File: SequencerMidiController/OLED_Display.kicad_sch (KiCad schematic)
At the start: 5 parts, among them J8 Conn_01x07

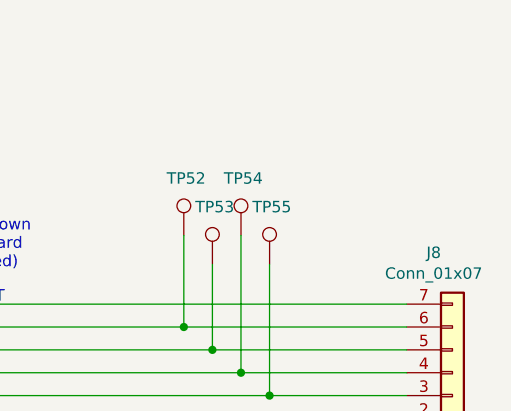
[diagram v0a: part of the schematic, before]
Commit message: Add ground points
https://github.com/cracked-machine/BassStationSequencerMidiController/issues/9

Also, made space on layout for uSDCard IDC connector and DAC analog output section
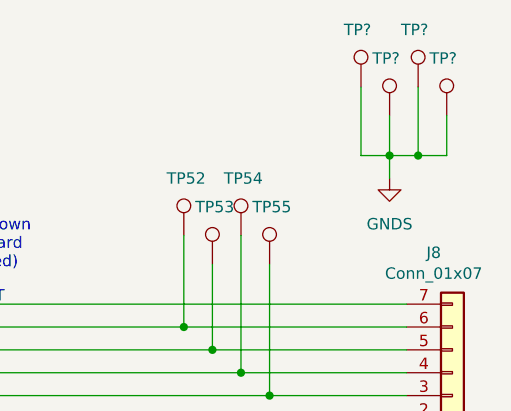
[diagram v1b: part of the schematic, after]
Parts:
- added TP? (x4): TestPoint, TestPoint:TestPoint_Pad_D1.0mm, symbol Connector:TestPoint
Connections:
- net GNDS: now also TP?.1, TP?.1, TP?.1, TP?.1
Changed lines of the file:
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@@
   (junction (at 130.81 86.36) (diameter 0) (color 0 0 0 0)
   )
+  (junction (at 153.67 64.77) (diameter 0) (color 0 0 0 0)
+  )
   (junction (at 133.985 88.9) (diameter 0) (color 0 0 0 0)
+  )
+  (junction (at 150.495 64.77) (diameter 0) (color 0 0 0 0)
   )
   (no_connect (at 87.63 81.28))
@@
     (stroke (width 0) (type default) (color 0 0 0 0))
   )
+  (wire (pts (xy 150.495 64.77) (xy 153.67 64.77))
+    (stroke (width 0) (type default) (color 0 0 0 0))
+  )
   (wire (pts (xy 152.4 83.82) (xy 127.635 83.82))
     (stroke (width 0) (type default) (color 0 0 0 0))
   )
+  (wire (pts (xy 156.845 64.77) (xy 156.845 60.325))
+    (stroke (width 0) (type default) (color 0 0 0 0))
+  )
   (wire (pts (xy 152.4 93.98) (xy 87.63 93.98))
     (stroke (width 0) (type default) (color 0 0 0 0))
   )
+  (wire (pts (xy 147.32 64.77) (xy 150.495 64.77))
+    (stroke (width 0) (type default) (color 0 0 0 0))
+  )
   (wire (pts (xy 133.985 88.9) (xy 87.63 88.9))
     (stroke (width 0) (type default) (color 0 0 0 0))
   )
+  (wire (pts (xy 150.495 60.325) (xy 150.495 64.77))
+    (stroke (width 0) (type default) (color 0 0 0 0))
+  )
+  (wire (pts (xy 153.67 64.77) (xy 156.845 64.77))
+    (stroke (width 0) (type default) (color 0 0 0 0))
+  )
   (wire (pts (xy 152.4 88.9) (xy 133.985 88.9))
     (stroke (width 0) (type default) (color 0 0 0 0))
   )
+  (wire (pts (xy 147.32 57.15) (xy 147.32 64.77))
+    (stroke (width 0) (type default) (color 0 0 0 0))
+  )
   (wire (pts (xy 87.63 81.28) (xy 152.4 81.28))
     (stroke (width 0) (type default) (color 0 0 0 0))
@@
     (stroke (width 0) (type default) (color 0 0 0 0))
   )
+  (wire (pts (xy 153.67 57.15) (xy 153.67 64.77))
+    (stroke (width 0) (type default) (color 0 0 0 0))
+  )
   (wire (pts (xy 152.4 96.52) (xy 111.76 96.52))
     (stroke (width 0) (type default) (color 0 0 0 0))
@@
   )
   (wire (pts (xy 152.4 91.44) (xy 137.16 91.44))
+    (stroke (width 0) (type default) (color 0 0 0 0))
+  )
+  (wire (pts (xy 150.495 64.77) (xy 150.495 67.31))
     (stroke (width 0) (type default) (color 0 0 0 0))
   )
@@
       (effects (font (size 1.27 1.27)) hide)
     )
+    (pin "1")
+  )
+  (symbol (lib_id "Connector:TestPoint") (at 150.495 60.325 0) (unit 1)
+    (in_bom yes) (on_board yes)
+    (property "Reference" "TP?" (id 0) (at 148.59 53.975 0)
+      (effects (font (size 1.27 1.27)) (justify left))
+    )
+    (property "Value" "TestPoint" (id 1) (at 151.9682 59.6392 0)
+      (effects (font (size 1.27 1.27)) (justify left) hide)
+    )
+    (property "Footprint" "TestPoint:TestPoint_Pad_D1.0mm" (id 2) (at 155.575 60.325 0)
+      (effects (font (size 1.27 1.27)) hide)
+    )
+    (property "Datasheet" "~" (id 3) (at 155.575 60.325 0)
+      (effects (font (size 1.27 1.27)) hide)
+    )
+    (property "LcscNo" "~" (id 4) (at 150.495 60.325 0)
+      (effects (font (size 1.27 1.27)) hide)
+    )
+    (property "Type" "~" (id 5) (at 150.495 60.325 0)
+      (effects (font (size 1.27 1.27)) hide)
+    )
+    (pin "1")
+  )
+  (symbol (lib_id "Connector:TestPoint") (at 156.845 60.325 0) (unit 1)
+    (in_bom yes) (on_board yes)
+    (property "Reference" "TP?" (id 0) (at 154.94 53.975 0)
+      (effects (font (size 1.27 1.27)) (justify left))
+    )
+    (property "Value" "TestPoint" (id 1) (at 158.3182 59.6392 0)
+      (effects (font (size 1.27 1.27)) (justify left) hide)
+    )
+    (property "Footprint" "TestPoint:TestPoint_Pad_D1.0mm" (id 2) (at 161.925 60.325 0)
+      (effects (font (size 1.27 1.27)) hide)
+    )
+    (property "Datasheet" "~" (id 3) (at 161.925 60.325 0)
+      (effects (font (size 1.27 1.27)) hide)
+    )
+    (property "LcscNo" "~" (id 4) (at 156.845 60.325 0)
+      (effects (font (size 1.27 1.27)) hide)
+    )
+    (property "Type" "~" (id 5) (at 156.845 60.325 0)
+      (effects (font (size 1.27 1.27)) hide)
+    )
+    (pin "1")
+  )
+  (symbol (lib_id "Connector:TestPoint") (at 153.67 57.15 0) (unit 1)
+    (in_bom yes) (on_board yes)
+    (property "Reference" "TP?" (id 0) (at 151.765 50.8 0)
+      (effects (font (size 1.27 1.27)) (justify left))
+    )
+    (property "Value" "TestPoint" (id 1) (at 155.1432 56.4642 0)
+      (effects (font (size 1.27 1.27)) (justify left) hide)
+    )
+    (property "Footprint" "TestPoint:TestPoint_Pad_D1.0mm" (id 2) (at 158.75 57.15 0)
+      (effects (font (size 1.27 1.27)) hide)
+    )
+    (property "Datasheet" "~" (id 3) (at 158.75 57.15 0)
+      (effects (font (size 1.27 1.27)) hide)
+    )
+    (property "LcscNo" "~" (id 4) (at 153.67 57.15 0)
+      (effects (font (size 1.27 1.27)) hide)
+    )
+    (property "Type" "~" (id 5) (at 153.67 57.15 0)
+      (effects (font (size 1.27 1.27)) hide)
+    )
+    (pin "1")
+  )
+  (symbol (lib_id "Connector:TestPoint") (at 147.32 57.15 0) (unit 1)
+    (in_bom yes) (on_board yes)
+    (property "Reference" "TP?" (id 0) (at 145.415 50.8 0)
+      (effects (font (size 1.27 1.27)) (justify left))
+    )
+    (property "Value" "TestPoint" (id 1) (at 148.7932 56.4642 0)
+      (effects (font (size 1.27 1.27)) (justify left) hide)
+    )
+    (property "Footprint" "TestPoint:TestPoint_Pad_D1.0mm" (id 2) (at 152.4 57.15 0)
+      (effects (font (size 1.27 1.27)) hide)
+    )
+    (property "Datasheet" "~" (id 3) (at 152.4 57.15 0)
+      (effects (font (size 1.27 1.27)) hide)
+    )
+    (property "LcscNo" "~" (id 4) (at 147.32 57.15 0)
+      (effects (font (size 1.27 1.27)) hide)
+    )
+    (property "Type" "~" (id 5) (at 147.32 57.15 0)
+      (effects (font (size 1.27 1.27)) hide)
+    )
+    (pin "1")
+  )
+  (symbol (lib_id "power:GNDS") (at 150.495 67.31 0) (unit 1)
+    (in_bom yes) (on_board yes) (fields_autoplaced)
+    (property "Reference" "#PWR?" (id 0) (at 150.495 73.66 0)
+      (effects (font (size 1.27 1.27)) hide)
+    )
+    (property "Value" "GNDS" (id 1) (at 150.495 72.39 0))
+    (property "Footprint" "" (id 2) (at 150.495 67.31 0)
+      (effects (font (size 1.27 1.27)) hide)
+    )
+    (property "Datasheet" "" (id 3) (at 150.495 67.31 0)
+      (effects (font (size 1.27 1.27)) hide)
+    )

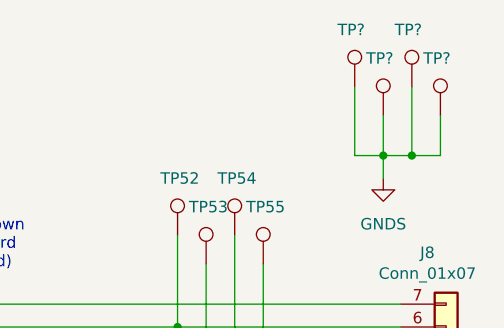
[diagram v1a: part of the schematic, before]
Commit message: updated layout DRC
Fixed clearance errors with polygons and pads in switch footprints
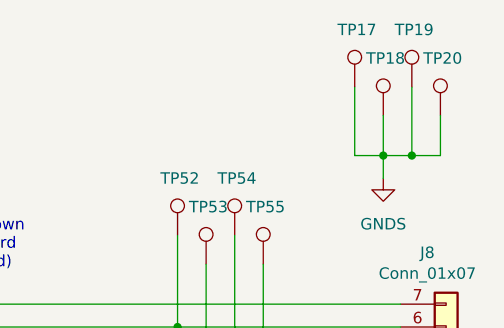
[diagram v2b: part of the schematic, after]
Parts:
- gave numbers to parts that had none: 4
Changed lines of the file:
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@@
   (symbol (lib_id "Connector:TestPoint") (at 150.495 60.325 0) (unit 1)
     (in_bom yes) (on_board yes)
-    (property "Reference" "TP?" (id 0) (at 148.59 53.975 0)
+    (property "Reference" "TP18" (id 0) (at 148.59 53.975 0)
       (effects (font (size 1.27 1.27)) (justify left))
     )
@@
   (symbol (lib_id "Connector:TestPoint") (at 156.845 60.325 0) (unit 1)
     (in_bom yes) (on_board yes)
-    (property "Reference" "TP?" (id 0) (at 154.94 53.975 0)
+    (property "Reference" "TP20" (id 0) (at 154.94 53.975 0)
       (effects (font (size 1.27 1.27)) (justify left))
     )
@@
   (symbol (lib_id "Connector:TestPoint") (at 153.67 57.15 0) (unit 1)
     (in_bom yes) (on_board yes)
-    (property "Reference" "TP?" (id 0) (at 151.765 50.8 0)
+    (property "Reference" "TP19" (id 0) (at 151.765 50.8 0)
       (effects (font (size 1.27 1.27)) (justify left))
     )
@@
   (symbol (lib_id "Connector:TestPoint") (at 147.32 57.15 0) (unit 1)
     (in_bom yes) (on_board yes)
-    (property "Reference" "TP?" (id 0) (at 145.415 50.8 0)
+    (property "Reference" "TP17" (id 0) (at 145.415 50.8 0)
       (effects (font (size 1.27 1.27)) (justify left))
     )
@@
   (symbol (lib_id "power:GNDS") (at 150.495 67.31 0) (unit 1)
     (in_bom yes) (on_board yes) (fields_autoplaced)
-    (property "Reference" "#PWR?" (id 0) (at 150.495 73.66 0)
+    (property "Reference" "#PWR0111" (id 0) (at 150.495 73.66 0)
       (effects (font (size 1.27 1.27)) hide)
     )
